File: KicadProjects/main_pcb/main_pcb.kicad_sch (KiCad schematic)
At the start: 0 parts

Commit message: finished schematic for main board
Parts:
- added 3.3V, 5V, Sensor: Conn_01x04_Socket, symbol Connector:Conn_01x04_Socket
- added Battery: 2462, 2462_KEY, symbol 2026-03-04_19-58-59:2462
- added LCD, Programmer_Pins: Conn_01x04_Pin, symbol Connector:Conn_01x04_Pin
- added LED_MOSFET, LED_PWM: LED_0805_Red, PCM_LED_SMD_AKL:LED_0805_2012Metric, symbol PCM_LED_AKL:LED_0805_Red
- added MOSFET: BS170FTA, SOT-23_DIO, symbol 2026-03-04_20-04-54:BS170FTA
- added Potent.: 3362P-1-103LF, POT_3362P, symbol 2026-03-04_19-59-54:3362P-1-103LF
- added R1, R2, R4: 1k, PCM_Resistor_SMD_AKL:R_1206_3216Metric, symbol PCM_Resistor_US_AKL:R_1206
- added R3: 510, PCM_Resistor_SMD_AKL:R_1206_3216Metric, symbol PCM_Resistor_US_AKL:R_1206
- added R5, R6: 10k, PCM_Resistor_SMD_AKL:R_1206_3216Metric, symbol PCM_Resistor_US_AKL:R_1206
- added U1: MSP430G2553IPW20R, PW20, symbol 2026-03-04_19-56-09:MSP430G2553IPW20R
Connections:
- new net: LED_PWM.2 (A), R5.1
- new net: MOSFET.3 (D), R2.1
- new net: LED_MOSFET.1 (K), R2.2
- new net: R3.1, R4.1, U1.8 (P2.0/TA1.0)
- new net: R3.2, Sensor.Echo (Pin_3)
- new net: 3.3V.Vin, 5V.Vin, Battery.2
- new net: Potent..2, U1.2 (P1.0/TA0CLK/ACLK/A0/CA0)
- new net: 3.3V.Vout, LED_MOSFET.2 (A), Potent..3.3V, R6.2, U1.1 (DVCC)
- new net: 5V.Vout, LCD.5V (Pin_2), Sensor.5V (Pin_1)
- new net: Programmer_Pins.Reset (Pin_2), R6.1, U1.16 (*RST/NMI/SBWTDIO)
- new net: Programmer_Pins.Test (Pin_3), U1.17 (TEST/SBWTCK)
- new net: MOSFET.1 (G), R1.1
- new net: R1.2, U1.4 (P1.2/TA0.1/UCA0TXD/UCA0SIMO/A2/CA2)
- new net: Sensor.Trg. (Pin_2), U1.9 (P2.1/TA1.1)
- new net: LCD.SCL (Pin_4), U1.14 (P1.6/TA0.1/UCB0SOMI/UCB0SCL/A6/CA6/TDI/TCLK)
- new net: LCD.SDA (Pin_3), U1.15 (P1.7/CAOUT/UCB0SIMO/UCB0SDA/A7/CA7/TDO/TDI)
- new net: R5.2, U1.3 (P1.1/TA0.0/UCA0RXD/UCA0SOMI/A1/CA1)
- new net GNDPWR: 3.3V.GND, 5V.GND, Battery.1, LCD.GND (Pin_1), LED_PWM.1 (K), MOSFET.2 (S), Potent..GND, Programmer_Pins.GND (Pin_1), R4.2, Sensor.GND (Pin_4), U1.20 (DVSS)
- no-connect marks 0 -> 11
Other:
- company: (none) -> University of Central Florida
- title: (none) -> Main Board - Junior Design

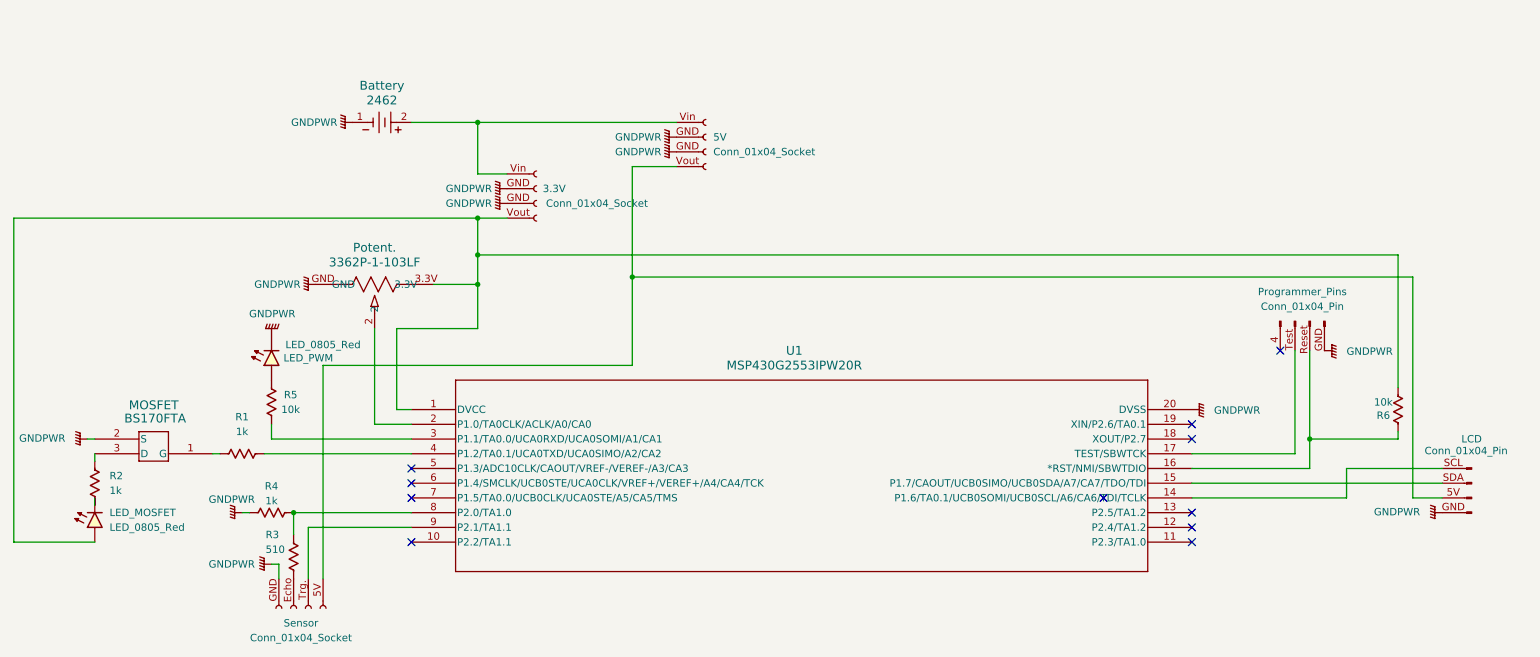
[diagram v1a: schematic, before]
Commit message: main board version 1 finished, awaiting review, no drc left
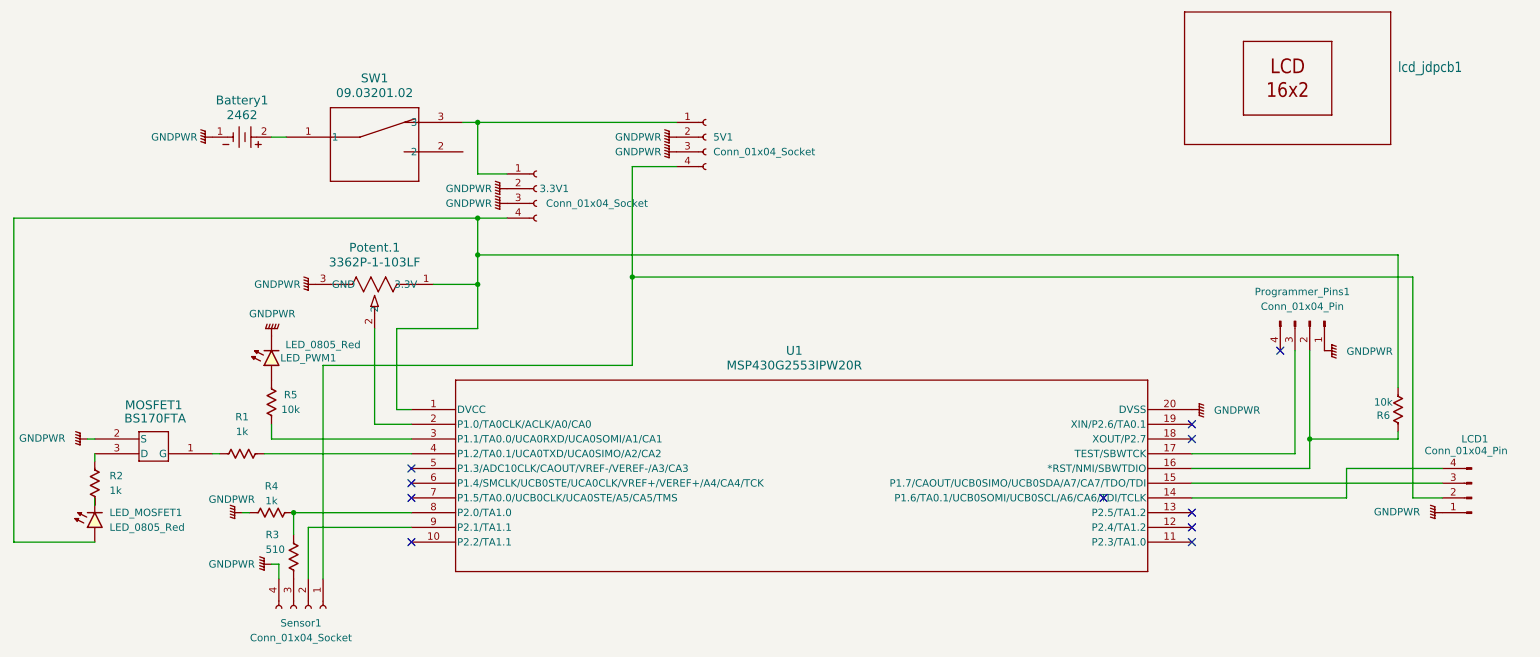
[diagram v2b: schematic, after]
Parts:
- added SW1: 09.03201.02, footprints:09.03201_EAO, symbol 2026-03-12_04-41-19:09.03201.02
- added lcd_jdpcb1: ~, jDPCB:JHD-162A, symbol LCD_DISP-6:LCD-16X2JHD-162A
- 3.3V1: renamed from 3.3V; footprint (none) -> footprints:CON4_1X4_TU_SSQ
- 5V1: renamed from 5V; footprint (none) -> footprints:CON4_1X4_TU_SSQ
- LCD1: renamed from LCD; footprint (none) -> Connector_PinHeader_2.54mm:PinHeader_1x04_P2.54mm_Vertical
- Programmer_Pins1: renamed from Programmer_Pins; footprint (none) -> Connector_PinHeader_2.54mm:PinHeader_1x04_P2.54mm_Vertical
- Sensor1: renamed from Sensor; footprint (none) -> footprints:CON4_1X4_TU_SSQ
- renumbered Battery to Battery1, LED_MOSFET to LED_MOSFET1, LED_PWM to LED_PWM1, MOSFET to MOSFET1, Potent. to Potent.1
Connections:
- net GNDPWR: now also 3.3V1.2 (GND), 3.3V1.3 (GND), 5V1.2 (GND), 5V1.3 (GND), LCD1.1 (GND), Potent.1.3 (GND), Programmer_Pins1.1 (GND), Sensor1.4 (GND); no longer 3.3V1.GND, 5V1.GND, LCD1.GND (Pin_1), Potent.1.GND, Programmer_Pins1.GND (Pin_1), Sensor1.GND (Pin_4)
- net at R3.2: now also Sensor1.3 (Echo); no longer Sensor1.Echo (Pin_3)
- net at LED_MOSFET1.2 (A), R6.2, U1.1 (DVCC): now also 3.3V1.4 (Vout), Potent.1.1 (3.3V); no longer 3.3V1.Vout, Potent.1.3.3V
- net at R6.1, U1.16 (*RST/NMI/SBWTDIO): now also Programmer_Pins1.2 (Reset); no longer Programmer_Pins1.Reset (Pin_2)
- net at U1.17 (TEST/SBWTCK): now also Programmer_Pins1.3 (Test); no longer Programmer_Pins1.Test (Pin_3)
- net at U1.9 (P2.1/TA1.1): now also Sensor1.2 (Trg.); no longer Sensor1.Trg. (Pin_2)
- net at U1.14 (P1.6/TA0.1/UCB0SOMI/UCB0SCL/A6/CA6/TDI/TCLK): now also LCD1.4 (SCL); no longer LCD1.SCL (Pin_4)
- net at U1.15 (P1.7/CAOUT/UCB0SIMO/UCB0SDA/A7/CA7/TDO/TDI): now also LCD1.3 (SDA); no longer LCD1.SDA (Pin_3)
- new net: Battery1.2, SW1.1
- new net: 3.3V1.1 (Vin), 5V1.1 (Vin), SW1.3
- new net: 5V1.4 (Vout), LCD1.2 (5V), Sensor1.1 (5V)
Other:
- moved on the sheet: Battery1, Programmer_Pins1

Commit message: yup
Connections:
- net at 3.3V1.1 (Vin), 5V1.1 (Vin): now also SW1.2; no longer SW1.3
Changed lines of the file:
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@@
 	)
 	(junction
-		(at 105.41 54.61)
+		(at 105.41 59.69)
 		(diameter 0)
 		(color 0 0 0 0)
@@
 	(wire
 		(pts
+			(xy 102.87 59.69) (xy 105.41 59.69)
+		)
+		(stroke
+			(width 0)
+			(type default)
+		)
+	)
+	(wire
+		(pts
 			(xy 60.96 111.76) (xy 59.69 111.76)
 		)
@@
 	(wire
 		(pts
-			(xy 102.87 54.61) (xy 105.41 54.61)
-		)
-		(stroke
-			(width 0)
-			(type default)
-		)
-	)
-	(wire
-		(pts
 			(xy 266.7 119.38) (xy 266.7 81.28)
 		)
@@
 	(wire
 		(pts
-			(xy 105.41 54.61) (xy 105.41 63.5)
+			(xy 105.41 54.61) (xy 105.41 59.69)
 		)
 		(stroke
@@
 		)
 		(stroke
+			(width 0)
+			(type default)
+		)
+	)
+	(wire
+		(pts
+			(xy 105.41 59.69) (xy 105.41 63.5)
+		)
+		(stroke
